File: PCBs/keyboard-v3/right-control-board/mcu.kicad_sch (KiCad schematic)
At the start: 11 parts, among them M1 2206-100T, SW1 SW_DIP_x01, SW2 SW_DIP_x01, SW3 SW_DIP_x01, U1 STM32G0C1CEUx

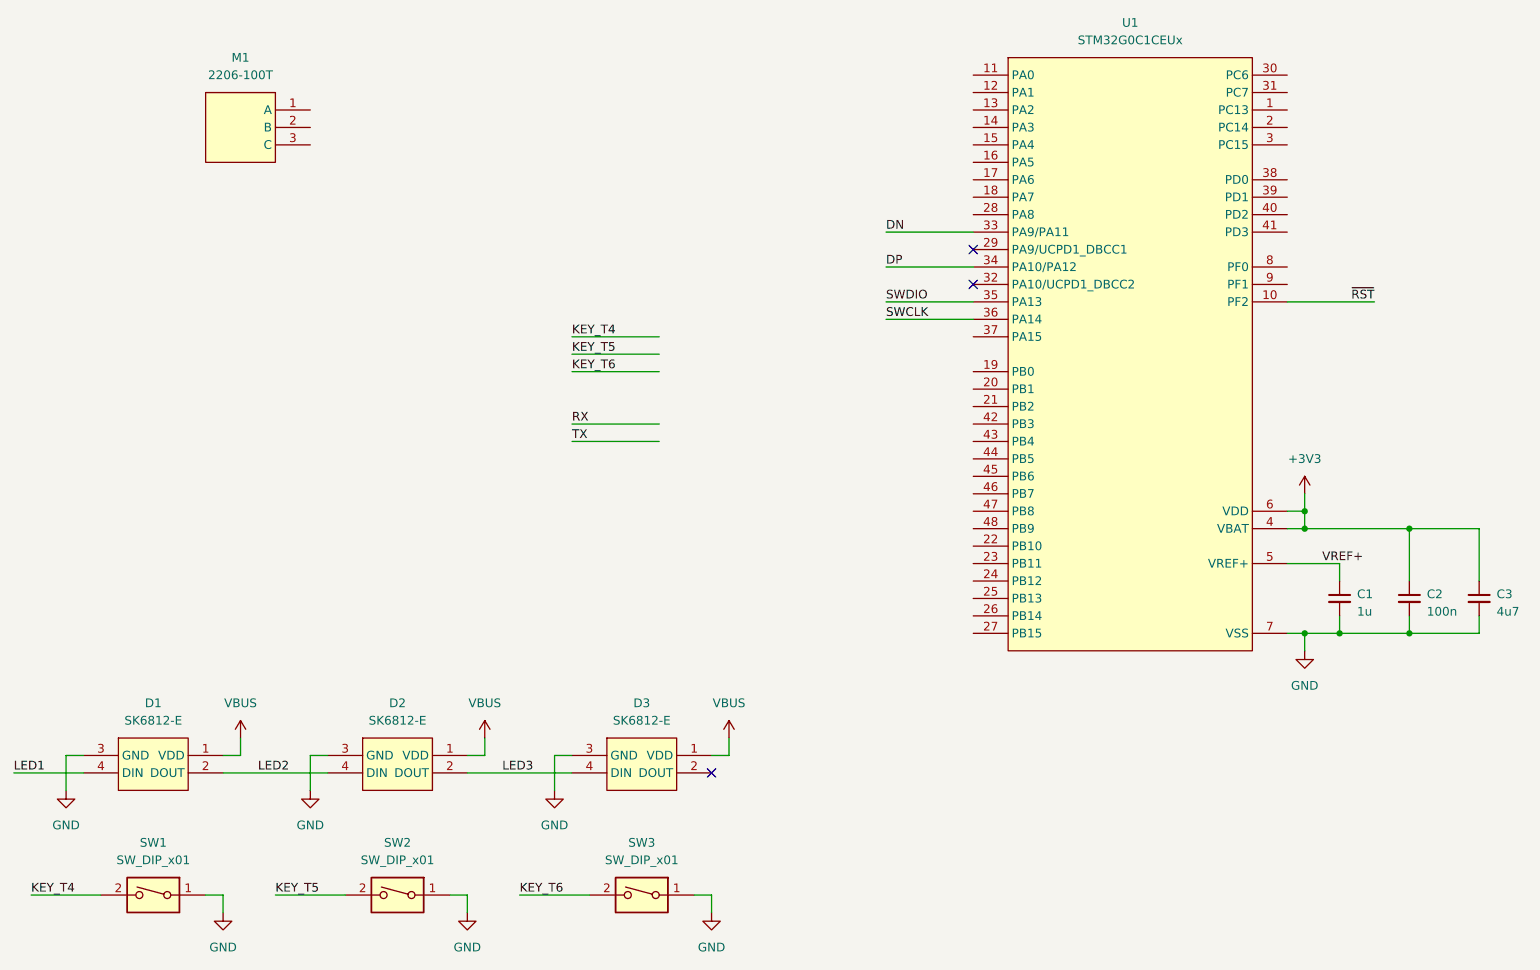
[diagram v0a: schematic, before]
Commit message: Right control board schematic almost done
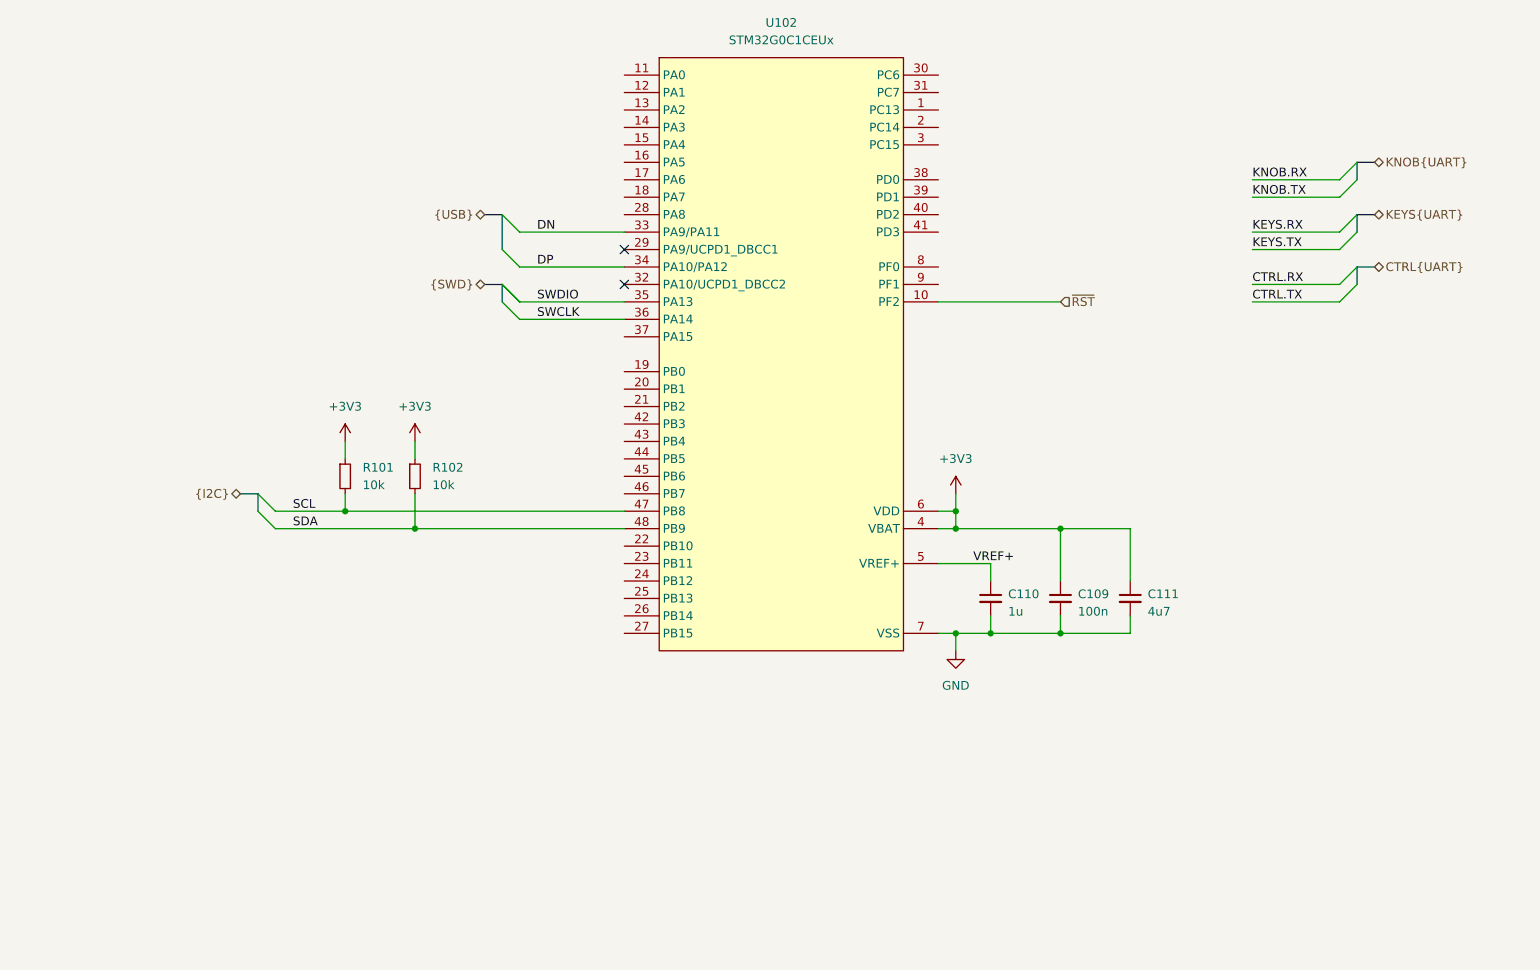
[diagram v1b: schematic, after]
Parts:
- removed D1, D2, D3: SK6812-E, project_footprints:sk6812-e, symbol LED:SK6812-E
- removed M1: 2206-100T, project_footprints:2206-100T, symbol MOTOR:2206-100T
- removed SW1, SW2, SW3: SW_DIP_x01, project_footprints:SW_Kailh_Choc_V1_HotSwap, symbol Switch:SW_DIP_x01
- added R101, R102: 10k, project_footprints:R_0402, symbol DEV:R_SMALL
- renumbered C2 to C109, C1 to C110, C3 to C111, U1 to U102
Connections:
- net +3V3: now also R101.1, R102.1
- net SCL: now reaches U102.47 (PB8)
- net SCL: now also R101.2
- net SDA: now reaches U102.48 (PB9)
- net SDA: now also R102.2
- no-connect marks 3 -> 2
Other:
- moved on the sheet: C109, C110, C111, U102

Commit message: Added debug-breakout board, progress on right side schematics & layout
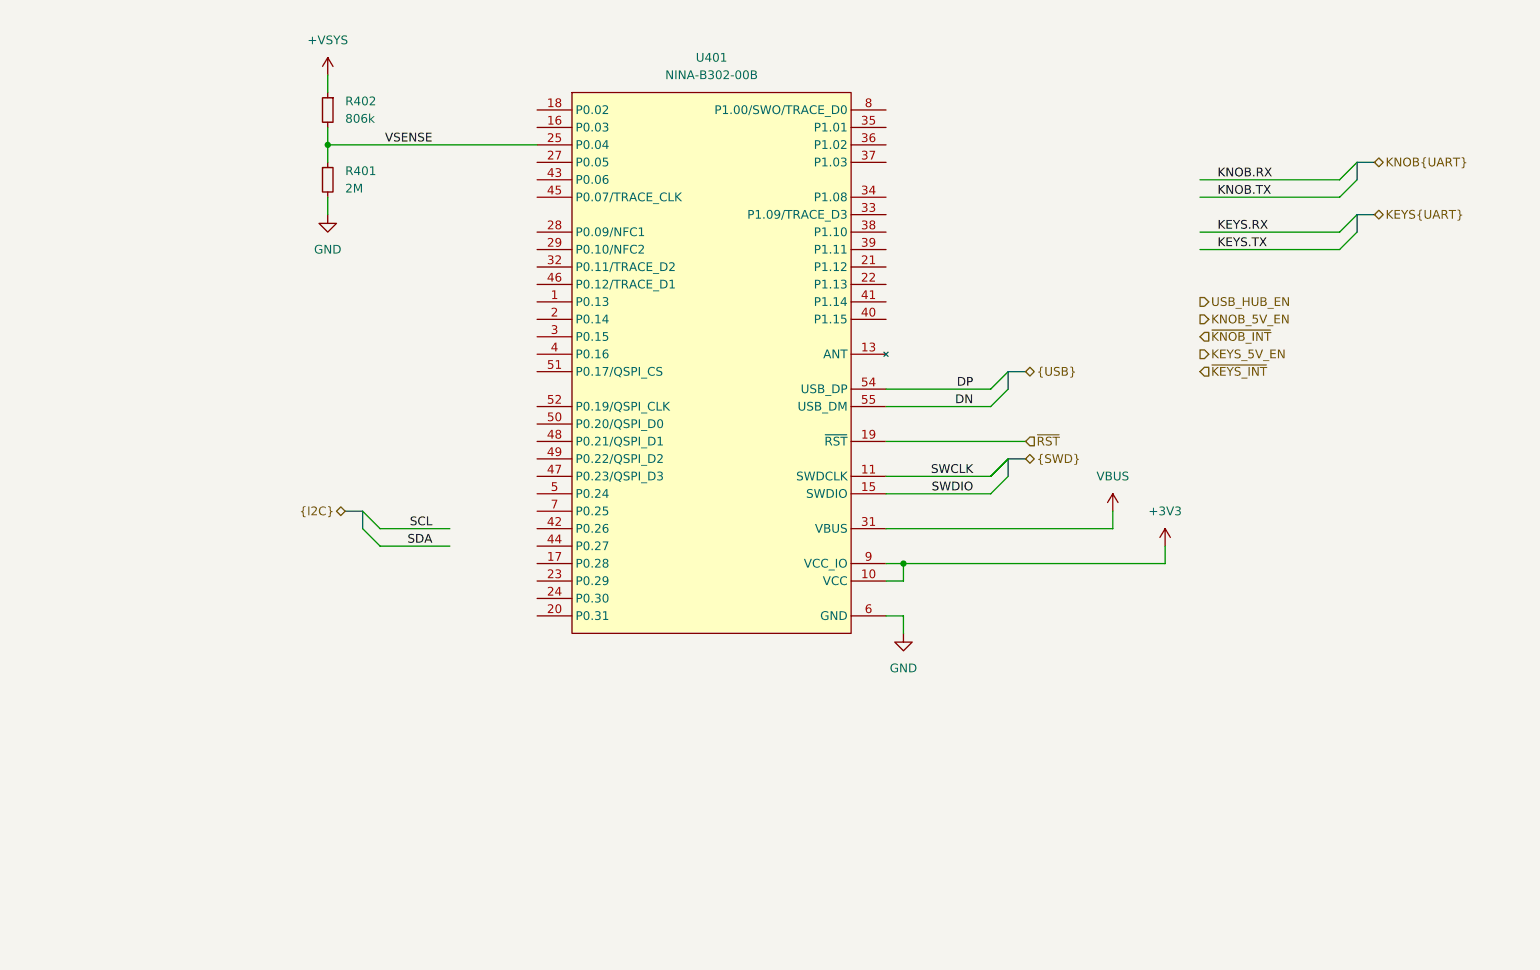
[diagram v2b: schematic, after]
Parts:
- removed C109: 100n, project_footprints:C_0402, symbol DEV:C_SMALL
- removed C110: 1u, project_footprints:C_0402, symbol DEV:C_SMALL
- removed C111: 4u7, project_footprints:C_0402, symbol DEV:C_SMALL
- removed R101, R102: 10k, project_footprints:R_0402, symbol DEV:R_SMALL
- removed U102: STM32G0C1CEUx, project_footprints:QFN50P700X700X60-49N-D, symbol STM32:STM32G0C1CEUx
- added R401: 2M, project_footprints:R_0402, symbol DEV:R_SMALL
- added R402: 806k, project_footprints:R_0402, symbol DEV:R_SMALL
- added U401: NINA-B302-00B, project_footprints:NINAB30200B, symbol NRF:NINA-B302-00B
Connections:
- net +3V3: now also U401.10 (VCC), U401.9 (VCC_IO)
- net DN: now also U401.55 (USB_DM)
- net DP: now also U401.54 (USB_DP)
- net GND: now also R401.2, U401.12 (GND), U401.14 (GND), U401.26 (GND), U401.30 (GND), U401.53 (GND), U401.56 (GND), U401.57 (GND), U401.58 (GND), U401.59 (GND), U401.6 (GND), U401.60 (GND), U401.61 (GND), U401.62 (GND), U401.63 (GND), U401.64 (GND), U401.65 (GND), U401.66 (GND), U401.67 (GND)
- net SWCLK: now also U401.11 (SWDCLK)
- net SWDIO: now also U401.15 (SWDIO)
- net ~{RST}: now also U401.19 (~{RST})
- new net +VSYS: R402.1
- new net VBUS: U401.31 (VBUS)
- new net VSENSE: R401.1, R402.2, U401.25 (P0.04)
- no-connect marks 2 -> 0

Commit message: Right control board placement and schematic done
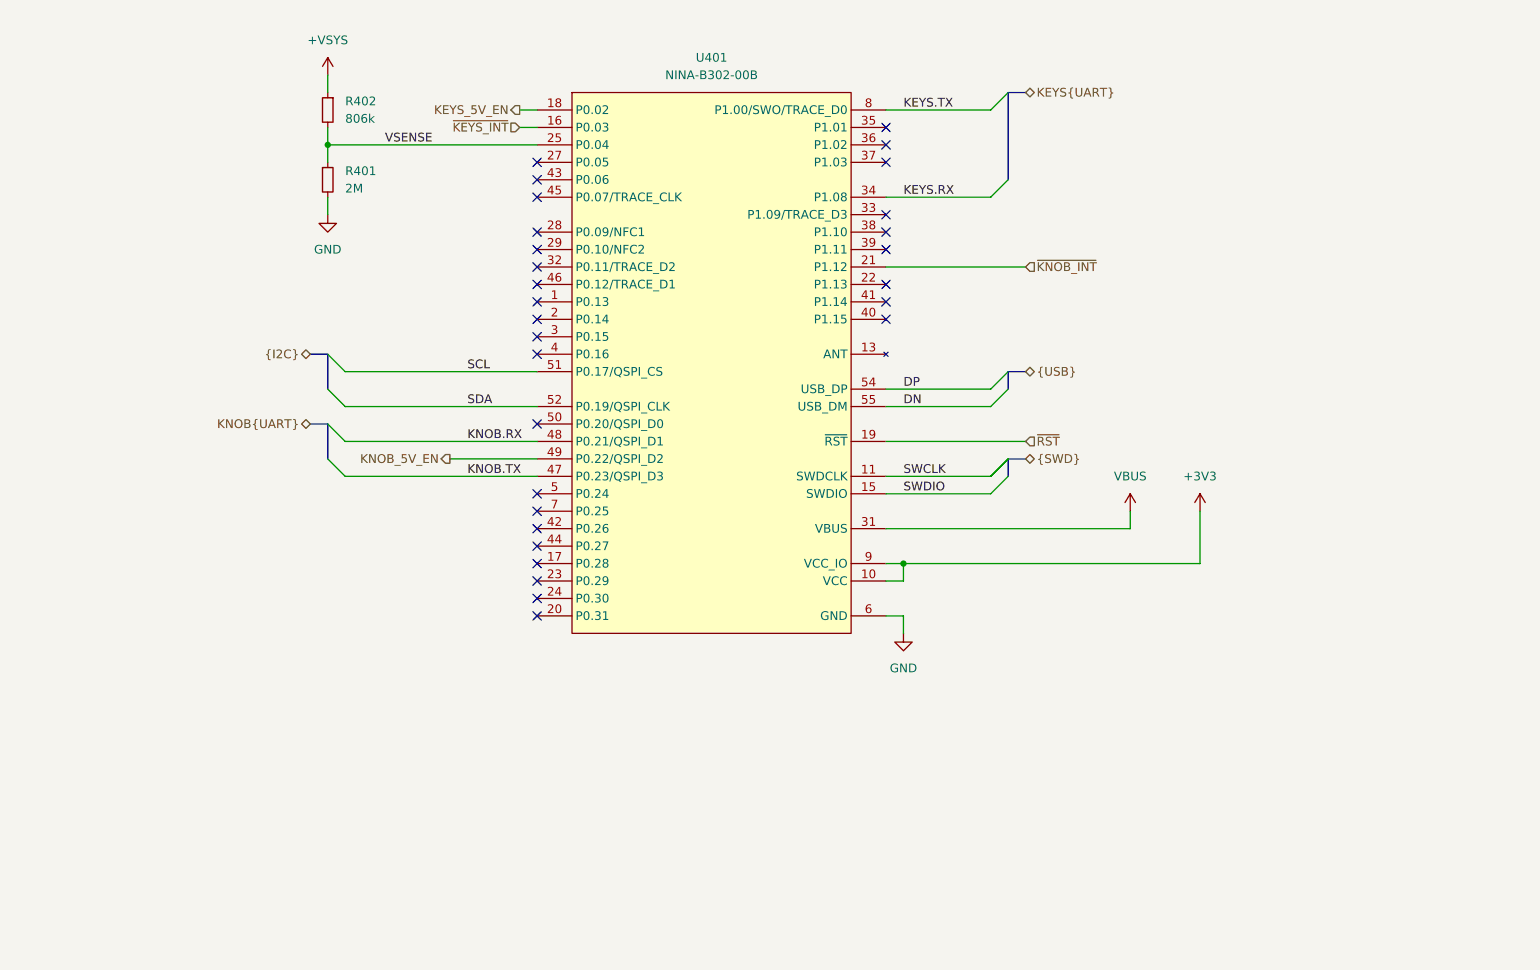
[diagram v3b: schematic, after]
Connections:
- net KEYS.RX: now also U401.34 (P1.08)
- net KEYS.TX: now also U401.8 (P1.00/SWO/TRACE_D0)
- net KEYS_5V_EN: now also U401.18 (P0.02)
- net KNOB.RX: now also U401.48 (P0.21/QSPI_D1)
- net KNOB.TX: now also U401.47 (P0.23/QSPI_D3)
- net KNOB_5V_EN: now also U401.49 (P0.22/QSPI_D2)
- net SCL: now also U401.51 (P0.17/QSPI_CS)
- net SDA: now also U401.52 (P0.19/QSPI_CLK)
- net ~{KEYS_INT}: now also U401.16 (P0.03)
- net ~{KNOB_INT}: now also U401.21 (P1.12)
- no-connect marks 0 -> 29

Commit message: Added mounting holes
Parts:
- renumbered R402 to R401, R401 to R402
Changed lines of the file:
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@@
 		(on_board yes)
 		(dnp no)
-		(property "Reference" "R402"
+		(property "Reference" "R401"
 			(at 88.9 57.1499 0)
 			(effects
@@
 			(project "right-control-board"
 				(path "/982f1c46-f6d6-42a2-bf2a-9fb0e913f11f/a8cedd16-275b-435b-a1f3-f83ccf5a22eb"
-					(reference "R402")
+					(reference "R401")
 					(unit 1)
 				)
@@
 		(on_board yes)
 		(dnp no)
-		(property "Reference" "R401"
+		(property "Reference" "R402"
 			(at 88.9 67.3099 0)
 			(effects
@@
 			(project "right-control-board"
 				(path "/982f1c46-f6d6-42a2-bf2a-9fb0e913f11f/a8cedd16-275b-435b-a1f3-f83ccf5a22eb"
-					(reference "R401")
+					(reference "R402")
 					(unit 1)
 				)
@@
 		(dnp no)
 		(fields_autoplaced yes)
-		(property "Reference" "#PWR0402"
+		(property "Reference" "#PWR0404"
 			(at 213.36 120.65 0)
 			(effects
@@
 			(project "right-control-board"
 				(path "/982f1c46-f6d6-42a2-bf2a-9fb0e913f11f/a8cedd16-275b-435b-a1f3-f83ccf5a22eb"
-					(reference "#PWR0402")
+					(reference "#PWR0404")
 					(unit 1)
 				)
@@
 		(dnp no)
 		(fields_autoplaced yes)
-		(property "Reference" "#PWR0404"
+		(property "Reference" "#PWR0405"
 			(at 170.18 140.97 0)
 			(effects
@@
 			(project "right-control-board"
 				(path "/982f1c46-f6d6-42a2-bf2a-9fb0e913f11f/a8cedd16-275b-435b-a1f3-f83ccf5a22eb"
-					(reference "#PWR0404")
+					(reference "#PWR0405")
 					(unit 1)
 				)
@@
 		(dnp no)
 		(fields_autoplaced yes)
-		(property "Reference" "#PWR0405"
+		(property "Reference" "#PWR0402"
 			(at 86.36 80.01 0)
 			(effects
@@
 			(project "right-control-board"
 				(path "/982f1c46-f6d6-42a2-bf2a-9fb0e913f11f/a8cedd16-275b-435b-a1f3-f83ccf5a22eb"
-					(reference "#PWR0405")
-					(unit 1)
-				)
+					(reference "#PWR0402")
+					(unit 1)
+				)
